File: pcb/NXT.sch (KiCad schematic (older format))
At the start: 8 parts, among them J3 NXT_RJ12, Q1 2N7002P

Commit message: Reannoted everything so that there isn't any duplicates. Also added connection to the rf reset line.
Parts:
- renumbered J3 to J1, R6 to R3, R7 to R4, R8 to R5, R29 to R6, R30 to R7
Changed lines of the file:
@@
-EESchema Schematic File Version 2  date 10/8/2012 8:27:48 PM
+EESchema Schematic File Version 2  date 10/11/2012 11:52:24 AM
 LIBS:power
 LIBS:device
@@
 Sheet 3 7
 Title ""
-Date "9 oct 2012"
+Date "11 oct 2012"
 Rev ""
 Comp ""
@@
 	8700 3500 8700 3800
 $Comp
-L RES R30
+L RES R7
 U 1 1 50736D94
 P 9000 3350
-F 0 "R30" H 9070 3315 50  0000 L TNN
+F 0 "R7" H 9070 3315 50  0000 L TNN
 F 1 "82k" H 9000 3405 30  0000 C BNN
 	1    9000 3350
@@
 $EndComp
 $Comp
-L RES R29
+L RES R6
 U 1 1 50736D91
 P 8700 3350
-F 0 "R29" H 8770 3315 50  0000 L TNN
+F 0 "R6" H 8770 3315 50  0000 L TNN
 F 1 "82k" H 8700 3405 30  0000 C BNN
 	1    8700 3350
@@
 EN_POW_9V
 $Comp
-L NXT_RJ12 J3
+L NXT_RJ12 J1
 U 1 1 5073673A
 P 7250 3900
-F 0 "J3" H 7450 4400 60  0000 C CNN
+F 0 "J1" H 7450 4400 60  0000 C CNN
 F 1 "NXT_RJ12" H 7100 4400 60  0000 C CNN
 	1    7250 3900
@@
 $EndComp
 $Comp
-L GND #PWR11
+L GND #PWR12
 U 1 1 50736739
 P 7200 3300
-F 0 "#PWR11" H 7200 3300 30  0001 C CNN
+F 0 "#PWR12" H 7200 3300 30  0001 C CNN
 F 1 "GND" H 7200 3230 30  0001 C CNN
 	1    7200 3300
@@
 $EndComp
 $Comp
-L RES R6
+L RES R3
 U 1 1 50736737
 P 4050 3950
-F 0 "R6" H 4120 3915 50  0000 L TNN
+F 0 "R3" H 4120 3915 50  0000 L TNN
 F 1 "100k" H 4050 4005 30  0000 C BNN
 	1    4050 3950
@@
 $EndComp
 $Comp
-L RES R8
+L RES R5
 U 1 1 50736736
 P 4900 3850
-F 0 "R8" H 4970 3815 50  0000 L TNN
+F 0 "R5" H 4970 3815 50  0000 L TNN
 F 1 "5k" H 4850 3900 30  0000 C BNN
 	1    4900 3850
@@
 Vreg
 $Comp
-L RES R7
+L RES R4
 U 1 1 50736734
 P 4550 3300
-F 0 "R7" H 4620 3265 50  0000 L TNN
+F 0 "R4" H 4620 3265 50  0000 L TNN
 F 1 "12k" H 4550 3355 30  0000 C BNN
 	1    4550 3300
@@
 Vnxt9v
 $Comp
-L GND #PWR10
+L GND #PWR11
 U 1 1 50736733
 P 4550 4250
-F 0 "#PWR10" H 4550 4250 30  0001 C CNN
+F 0 "#PWR11" H 4550 4250 30  0001 C CNN
 F 1 "GND" H 4550 4180 30  0001 C CNN
 	1    4550 4250

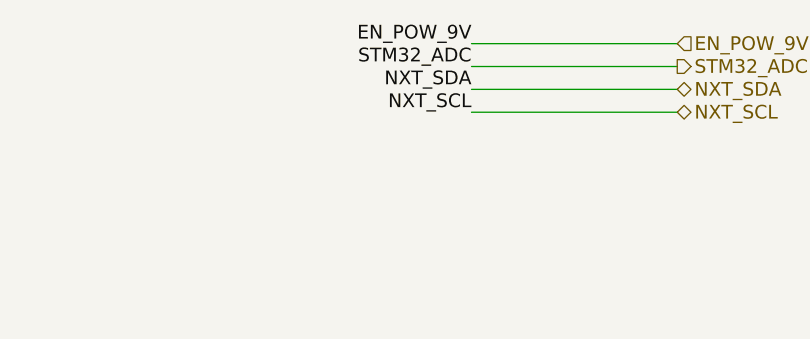
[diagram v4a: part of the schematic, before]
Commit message: Rearranged all the lines except for the power lines.
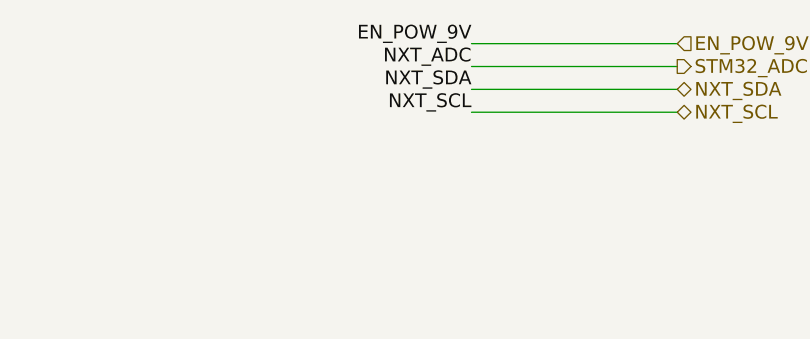
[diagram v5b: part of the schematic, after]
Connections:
- net labels added: NXT_ADC
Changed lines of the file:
@@
-EESchema Schematic File Version 2  date 12/16/2012 4:31:25 PM
+EESchema Schematic File Version 2  date 12/17/2012 11:02:29 PM
 LIBS:power
 LIBS:device
@@
 Sheet 7 9
 Title ""
-Date "16 dec 2012"
+Date "18 dec 2012"
 Rev ""
 Comp ""
@@
 NXT_SDA
 Text Label 8900 1150 2    60   ~ 0
-STM32_ADC
+NXT_ADC
 Text Label 8900 1050 2    60   ~ 0
 EN_POW_9V
